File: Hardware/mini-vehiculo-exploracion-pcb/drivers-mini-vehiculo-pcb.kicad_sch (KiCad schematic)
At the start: 25 parts, among them J1 Conn_01x08_Pin_drv, J2 Conn_01x02_Pin, J3 Conn_01x02_Motor1, J4 Conn_01x02_Motor2, J5 Conn_01x02_Battery, U3 DRV8873HPWPRQ1, U4 DRV8873HPWPRQ1

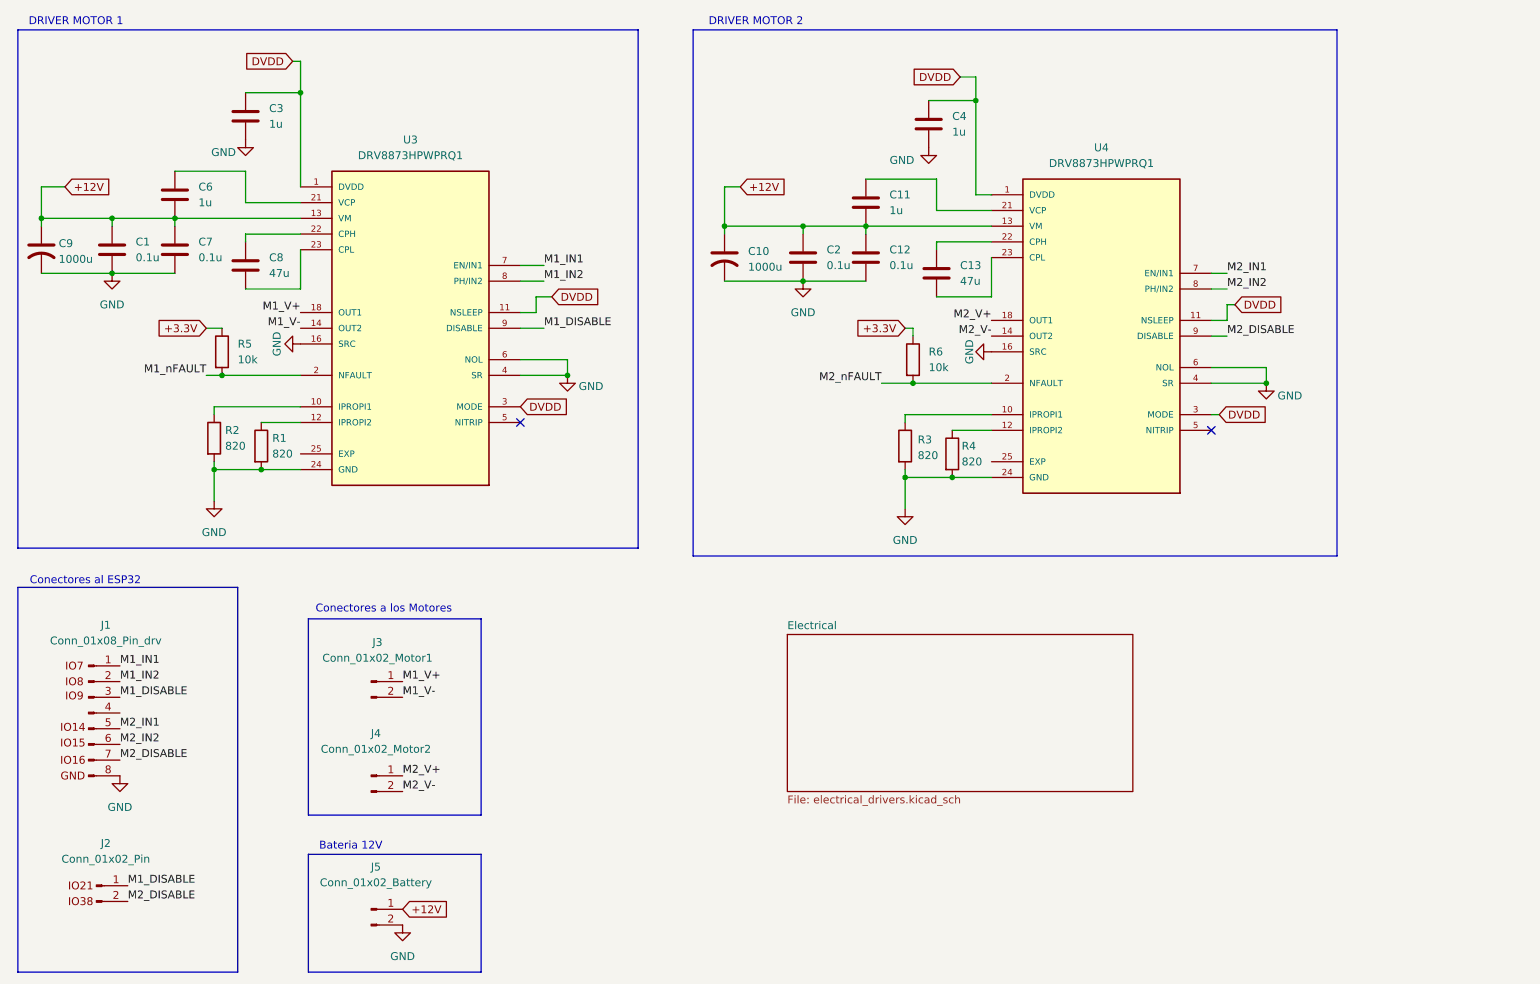
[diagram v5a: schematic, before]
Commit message: add capacitor footprints
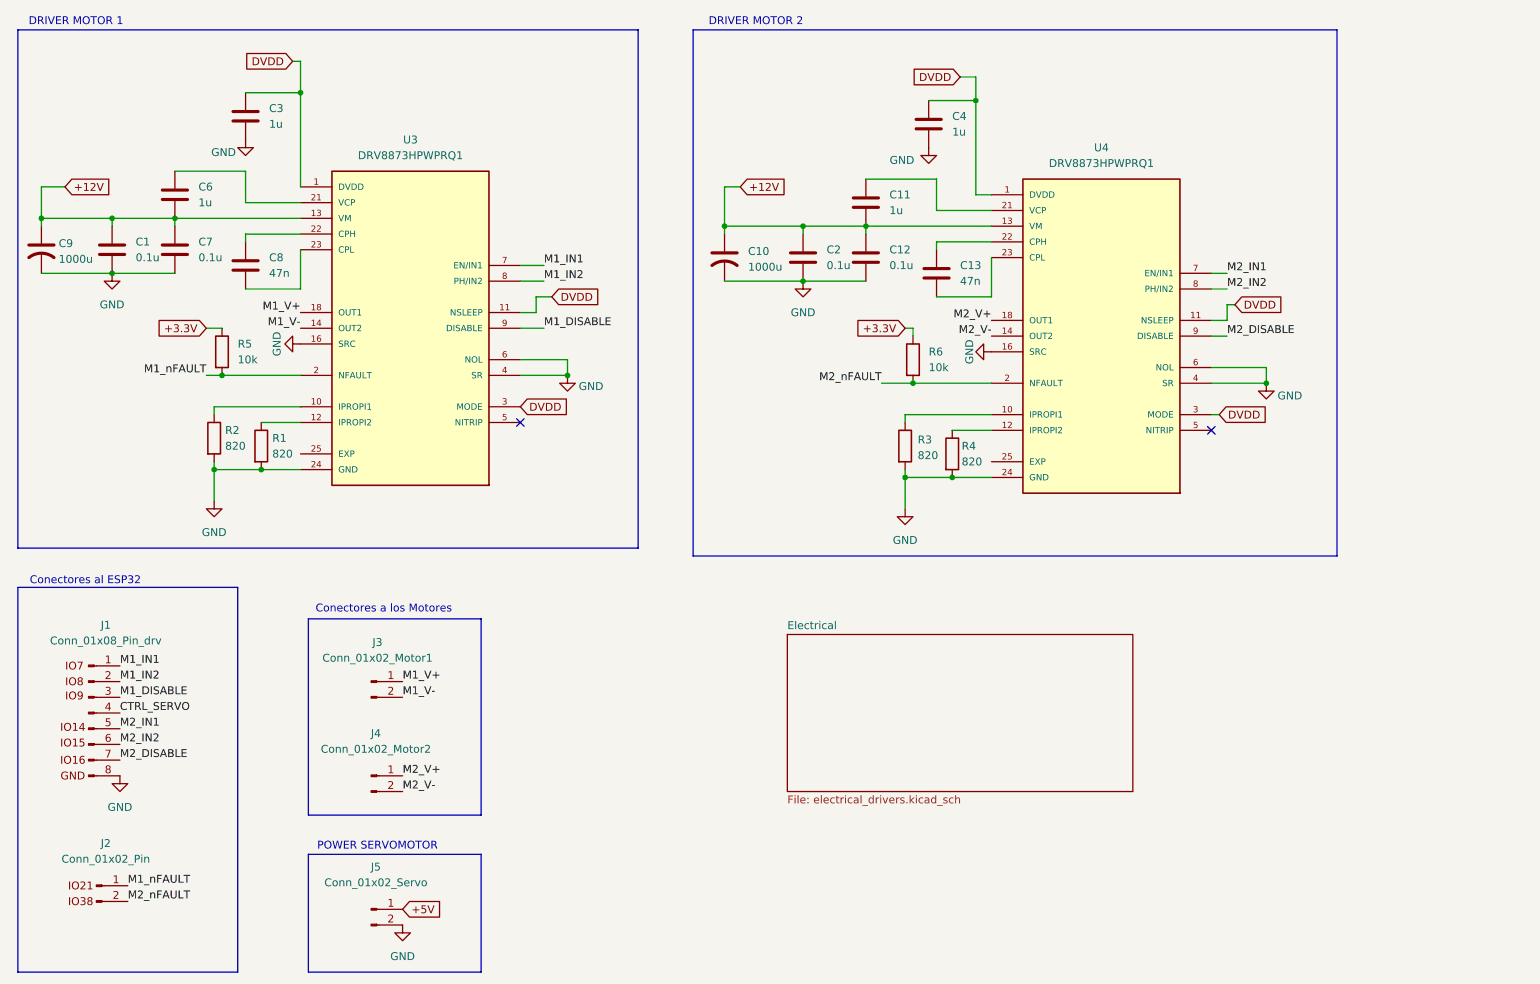
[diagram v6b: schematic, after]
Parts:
- C13, C8: value 47u -> 47n
- J5: value Conn_01x02_Battery -> Conn_01x02_Servo
- U3, U4: footprint DRV8873HPWPRQ1:SOP65P640X120-25N -> DRV8873HPWPRQ1:DRV8873HPWPRQ1
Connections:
- net M1_DISABLE: no longer J2.1 (Pin_1)
- net M1_nFAULT: now also J2.1 (Pin_1)
- net M2_DISABLE: no longer J2.2 (Pin_2)
- net M2_nFAULT: now also J2.2 (Pin_2)
- net VM: no longer J5.1 (Pin_1)
- net CTRL_SERVO: now reaches J1.4 (Pin_4)
- new net +5V: J5.1 (Pin_1)
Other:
- note added: "POWER SERVOMOTOR"
- note removed: "Bateria 12V"
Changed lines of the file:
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@@
 		)
 	)
-	(text "Bateria 12V"
+	(text "POWER SERVOMOTOR"
 		(exclude_from_sim no)
-		(at 83.058 166.37 0)
+		(at 87.376 166.37 0)
 		(effects
 			(font
@@
 		)
 	)
+	(label "CTRL_SERVO"
+		(at 45.72 144.78 0)
+		(effects
+			(font
+				(size 1.27 1.27)
+			)
+			(justify left bottom)
+		)
+	)
 	(label "M2_V-"
 		(at 186.69 83.82 180)
@@
 		)
 	)
-	(label "M1_DISABLE"
+	(label "M1_nFAULT"
 		(at 46.99 172.72 0)
 		(effects
@@
 		)
 	)
-	(label "M2_DISABLE"
+	(label "M2_nFAULT"
 		(at 46.99 175.26 0)
 		(effects
@@
 		)
 	)
-	(global_label "+12V"
+	(global_label "+5V"
 		(shape input)
 		(at 91.44 176.53 0)
@@
 		)
 		(property "Intersheetrefs" "${INTERSHEET_REFS}"
-			(at 99.5052 176.53 0)
+			(at 98.2957 176.53 0)
 			(effects
 				(font
@@
 			)
 		)
-		(property "Value" "Conn_01x02_Battery"
+		(property "Value" "Conn_01x02_Servo"
 			(at 87.122 172.212 0)
 			(effects
@@
 			)
 		)
-		(property "Footprint" "DRV8873HPWPRQ1:SOP65P640X120-25N"
+		(property "Footprint" "DRV8873HPWPRQ1:DRV8873HPWPRQ1"
 			(at 92.71 82.55 0)
 			(effects
@@
 			)
 		)
-		(property "Value" "47u"
+		(property "Value" "47n"
 			(at 69.85 73.6599 0)
 			(effects
@@
 			)
 		)
-		(property "Footprint" "DRV8873HPWPRQ1:SOP65P640X120-25N"
+		(property "Footprint" "DRV8873HPWPRQ1:DRV8873HPWPRQ1"
 			(at 204.47 83.82 0)
 			(effects
@@
 			)
 		)
-		(property "Value" "47u"
+		(property "Value" "47n"
 			(at 181.61 74.9299 0)
 			(effects

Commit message: updated driver pcb
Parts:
- C1, C11, C12, C2, C3, C4, C6, C7: footprint (none) -> capacitores_driver:CAPC2012X88N
- C13, C8: footprint (none) -> capacitores_driver:CAPC2012X140N
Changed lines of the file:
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@@
 			)
 		)
-		(property "Footprint" ""
+		(property "Footprint" "capacitores_driver:CAPC2012X88N"
 			(at 167.3352 66.04 0)
 			(effects
@@
 			)
 		)
-		(property "Footprint" ""
+		(property "Footprint" "capacitores_driver:CAPC2012X88N"
 			(at 167.3352 74.93 0)
 			(effects
@@
 			)
 		)
-		(property "Footprint" ""
+		(property "Footprint" "capacitores_driver:CAPC2012X88N"
 			(at 55.5752 64.77 0)
 			(effects
@@
 			)
 		)
-		(property "Footprint" ""
+		(property "Footprint" "capacitores_driver:CAPC2012X140N"
 			(at 67.0052 76.2 0)
 			(effects
@@
 			)
 		)
-		(property "Footprint" ""
+		(property "Footprint" "capacitores_driver:CAPC2012X88N"
 			(at 67.0052 52.07 0)
 			(effects
@@
 			)
 		)
-		(property "Footprint" ""
+		(property "Footprint" "capacitores_driver:CAPC2012X88N"
 			(at 177.4952 53.34 0)
 			(effects
@@
 			)
 		)
-		(property "Footprint" ""
+		(property "Footprint" "capacitores_driver:CAPC2012X88N"
 			(at 45.4152 73.66 0)
 			(effects
@@
 			)
 		)
-		(property "Footprint" ""
+		(property "Footprint" "capacitores_driver:CAPC2012X88N"
 			(at 55.5752 73.66 0)
 			(effects
@@
 			)
 		)
-		(property "Footprint" ""
+		(property "Footprint" "capacitores_driver:CAPC2012X88N"
 			(at 157.1752 74.93 0)
 			(effects
@@
 			)
 		)
-		(property "Footprint" ""
+		(property "Footprint" "capacitores_driver:CAPC2012X140N"
 			(at 178.7652 77.47 0)
 			(effects

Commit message: updated resistor footprint
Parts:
- R1, R2, R3, R4, R5, R6: footprint (none) -> Resistor_SMD:R_0805_2012Metric_Pad1.20x1.40mm_HandSolder
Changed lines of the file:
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@@
 			)
 		)
-		(property "Footprint" ""
+		(property "Footprint" "Resistor_SMD:R_0805_2012Metric_Pad1.20x1.40mm_HandSolder"
 			(at 59.182 100.33 90)
 			(effects
@@
 			)
 		)
-		(property "Footprint" ""
+		(property "Footprint" "Resistor_SMD:R_0805_2012Metric_Pad1.20x1.40mm_HandSolder"
 			(at 178.562 102.87 90)
 			(effects
@@
 			)
 		)
-		(property "Footprint" ""
+		(property "Footprint" "Resistor_SMD:R_0805_2012Metric_Pad1.20x1.40mm_HandSolder"
 			(at 66.802 101.6 90)
 			(effects
@@
 			)
 		)
-		(property "Footprint" ""
+		(property "Footprint" "Resistor_SMD:R_0805_2012Metric_Pad1.20x1.40mm_HandSolder"
 			(at 170.942 101.6 90)
 			(effects
@@
 			)
 		)
-		(property "Footprint" ""
+		(property "Footprint" "Resistor_SMD:R_0805_2012Metric_Pad1.20x1.40mm_HandSolder"
 			(at 60.452 86.36 90)
 			(effects
@@
 			)
 		)
-		(property "Footprint" ""
+		(property "Footprint" "Resistor_SMD:R_0805_2012Metric_Pad1.20x1.40mm_HandSolder"
 			(at 172.212 87.63 90)
 			(effects
